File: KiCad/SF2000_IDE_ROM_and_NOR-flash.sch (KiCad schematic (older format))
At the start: 6 parts, among them J5 IDE_ATA_44pin, U13 SST39LF040, U14 SST39LF802C, U15 74LVC245A, U16 74LVC245A, U17 74LVC245A

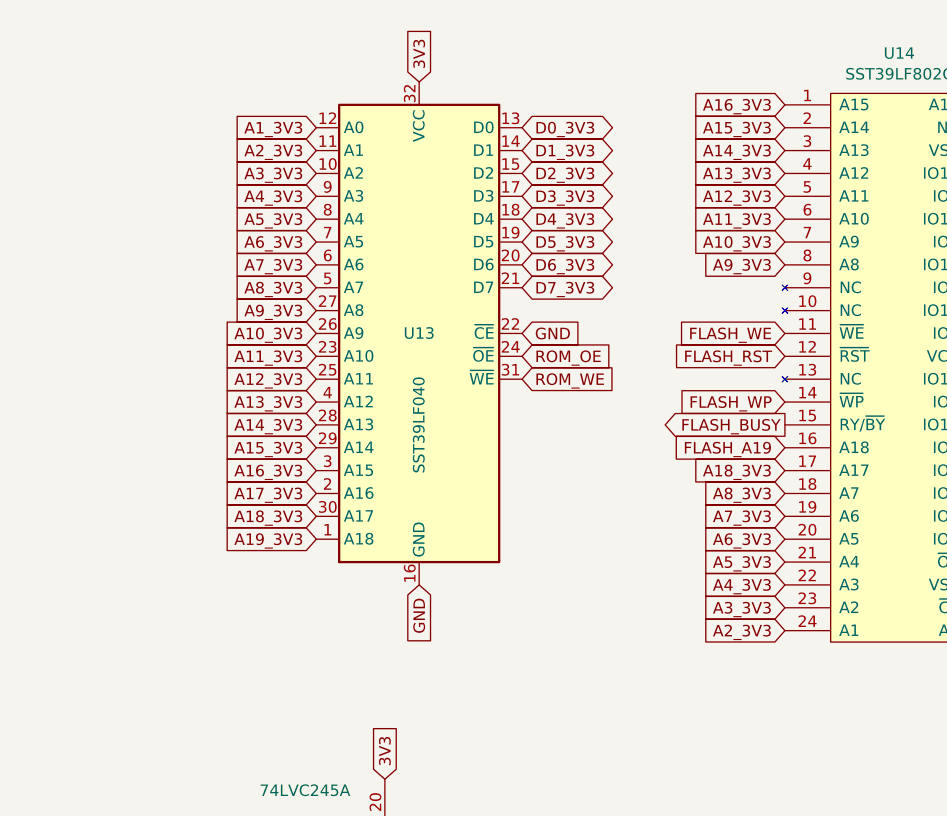
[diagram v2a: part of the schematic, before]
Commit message: added Oscillator, pull-up resistor and more routing done
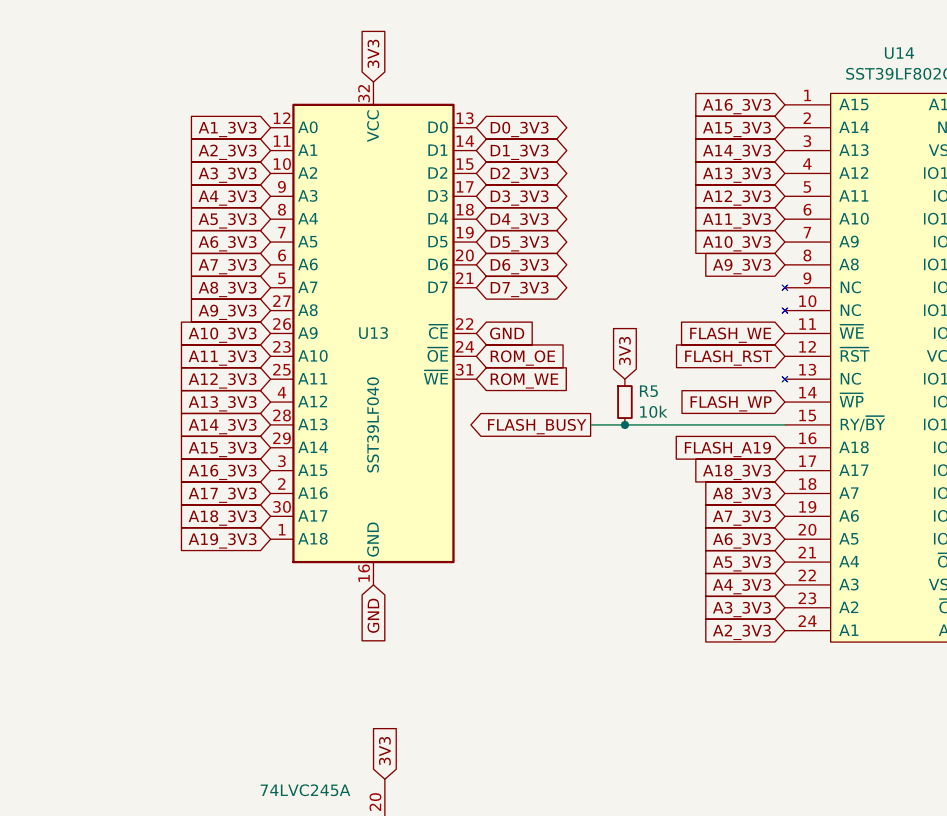
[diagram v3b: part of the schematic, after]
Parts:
- added R5: 10k, Resistor_SMD:R_0805_2012Metric_Pad1.15x1.40mm_HandSolder, symbol Device:R_Small
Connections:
- net 3V3: now also R5.1
- net FLASH_BUSY: now also R5.2
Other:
- moved on the sheet: U13
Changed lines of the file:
@@
 L SF2000:SST39LF040 U13
 U 1 1 627D2ECC
-P 6950 2600
-F 0 "U13" H 6950 2600 50  0000 C CNN
-F 1 "SST39LF040" V 6950 2200 50  0000 C CNN
-F 2 "SF2000:PLCC-32_11.4x14.0mm_P1.27mm" H 6950 2600 50  0001 C CNN
-F 3 "https://ww1.microchip.com/downloads/en/DeviceDoc/20005023B.pdf" H 6950 2700 50  0001 C CNN
-	1    6950 2600
+P 6750 2600
+F 0 "U13" H 6750 2600 50  0000 C CNN
+F 1 "SST39LF040" V 6750 2200 50  0000 C CNN
+F 2 "SF2000:PLCC-32_11.4x14.0mm_P1.27mm" H 6750 2600 50  0001 C CNN
+F 3 "https://ww1.microchip.com/downloads/en/DeviceDoc/20005023B.pdf" H 6750 2700 50  0001 C CNN
+	1    6750 2600
 	1    0    0    -1
 $EndComp
@@
 Text GLabel 9550 2700 2    50   Input ~ 0
 3V3
-Text GLabel 6500 2100 0    50   Input ~ 0
+Text GLabel 6300 2100 0    50   Input ~ 0
 A5_3V3
-Text GLabel 6500 2200 0    50   Input ~ 0
+Text GLabel 6300 2200 0    50   Input ~ 0
 A6_3V3
-Text GLabel 6500 2000 0    50   Input ~ 0
+Text GLabel 6300 2000 0    50   Input ~ 0
 A4_3V3
-Text GLabel 6500 1900 0    50   Input ~ 0
+Text GLabel 6300 1900 0    50   Input ~ 0
 A3_3V3
-Text GLabel 6500 2300 0    50   Input ~ 0
+Text GLabel 6300 2300 0    50   Input ~ 0
 A7_3V3
-Text GLabel 6500 2400 0    50   Input ~ 0
+Text GLabel 6300 2400 0    50   Input ~ 0
 A8_3V3
-Text GLabel 6500 1800 0    50   Input ~ 0
+Text GLabel 6300 1800 0    50   Input ~ 0
 A2_3V3
-Text GLabel 6500 1700 0    50   Input ~ 0
+Text GLabel 6300 1700 0    50   Input ~ 0
 A1_3V3
-Text GLabel 6500 2700 0    50   Input ~ 0
+Text GLabel 6300 2700 0    50   Input ~ 0
 A11_3V3
-Text GLabel 6500 2500 0    50   Input ~ 0
+Text GLabel 6300 2500 0    50   Input ~ 0
 A9_3V3
-Text GLabel 6500 2600 0    50   Input ~ 0
+Text GLabel 6300 2600 0    50   Input ~ 0
 A10_3V3
-Text GLabel 6500 2800 0    50   Input ~ 0
+Text GLabel 6300 2800 0    50   Input ~ 0
 A12_3V3
-Text GLabel 6500 2900 0    50   Input ~ 0
+Text GLabel 6300 2900 0    50   Input ~ 0
 A13_3V3
-Text GLabel 6500 3000 0    50   Input ~ 0
+Text GLabel 6300 3000 0    50   Input ~ 0
 A14_3V3
-Text GLabel 6500 3100 0    50   Input ~ 0
+Text GLabel 6300 3100 0    50   Input ~ 0
 A15_3V3
-Text GLabel 6500 3200 0    50   Input ~ 0
+Text GLabel 6300 3200 0    50   Input ~ 0
 A16_3V3
-Text GLabel 6500 3300 0    50   Input ~ 0
+Text GLabel 6300 3300 0    50   Input ~ 0
 A17_3V3
 Text GLabel 9550 3500 2    50   BiDi ~ 0
@@
 Text GLabel 8550 2900 0    50   Input ~ 0
 FLASH_WP
-Text GLabel 8550 3000 0    50   Output ~ 0
+Text GLabel 7700 3000 0    50   Output ~ 0
 FLASH_BUSY
-Text GLabel 7400 2800 2    50   Input ~ 0
+Text GLabel 7200 2800 2    50   Input ~ 0
 ROM_WE
-Text GLabel 7400 2700 2    50   Input ~ 0
+Text GLabel 7200 2700 2    50   Input ~ 0
 ROM_OE
-Text GLabel 7400 2600 2    50   Input ~ 0
-GND
-Text GLabel 6950 3700 3    50   Input ~ 0
-GND
-Text GLabel 6950 1500 1    50   Input ~ 0
-3V3
-Text GLabel 6500 3400 0    50   Input ~ 0
+Text GLabel 7200 2600 2    50   Input ~ 0
+GND
+Text GLabel 6750 3700 3    50   Input ~ 0
+GND
+Text GLabel 6750 1500 1    50   Input ~ 0
+3V3
+Text GLabel 6300 3400 0    50   Input ~ 0
 A18_3V3
-Text GLabel 6500 3500 0    50   Input ~ 0
+Text GLabel 6300 3500 0    50   Input ~ 0
 A19_3V3
-Text GLabel 7400 1700 2    50   BiDi ~ 0
+Text GLabel 7200 1700 2    50   BiDi ~ 0
 D0_3V3
-Text GLabel 7400 1800 2    50   BiDi ~ 0
+Text GLabel 7200 1800 2    50   BiDi ~ 0
 D1_3V3
-Text GLabel 7400 1900 2    50   BiDi ~ 0
+Text GLabel 7200 1900 2    50   BiDi ~ 0
 D2_3V3
-Text GLabel 7400 2000 2    50   BiDi ~ 0
+Text GLabel 7200 2000 2    50   BiDi ~ 0
 D3_3V3
-Text GLabel 7400 2100 2    50   BiDi ~ 0
+Text GLabel 7200 2100 2    50   BiDi ~ 0
 D4_3V3
-Text GLabel 7400 2200 2    50   BiDi ~ 0
+Text GLabel 7200 2200 2    50   BiDi ~ 0
 D5_3V3
-Text GLabel 7400 2300 2    50   BiDi ~ 0
+Text GLabel 7200 2300 2    50   BiDi ~ 0
 D6_3V3
-Text GLabel 7400 2400 2    50   BiDi ~ 0
+Text GLabel 7200 2400 2    50   BiDi ~ 0
 D7_3V3
 Text GLabel 4400 4950 0    50   BiDi ~ 0
@@
 Text GLabel 3100 2550 2    50   BiDi ~ 0
 IDE_D15
+$Comp
+L Device:R_Small R5
+U 1 1 620512F9
+P 7850 2900
+F 0 "R5" H 7909 2946 50  0000 L CNN
+F 1 "10k" H 7909 2855 50  0000 L CNN
+F 2 "Resistor_SMD:R_0805_2012Metric_Pad1.15x1.40mm_HandSolder" H 7850 2900 50  0001 C CNN
+F 3 "~" H 7850 2900 50  0001 C CNN
+	1    7850 2900
+	1    0    0    -1
+$EndComp
+Wire Wire Line
+	7700 3000 7850 3000
+Connection ~ 7850 3000
+Wire Wire Line
+	7850 3000 8550 3000
+Text GLabel 7850 2800 1    50   Input ~ 0
+3V3
 $EndSCHEMATC

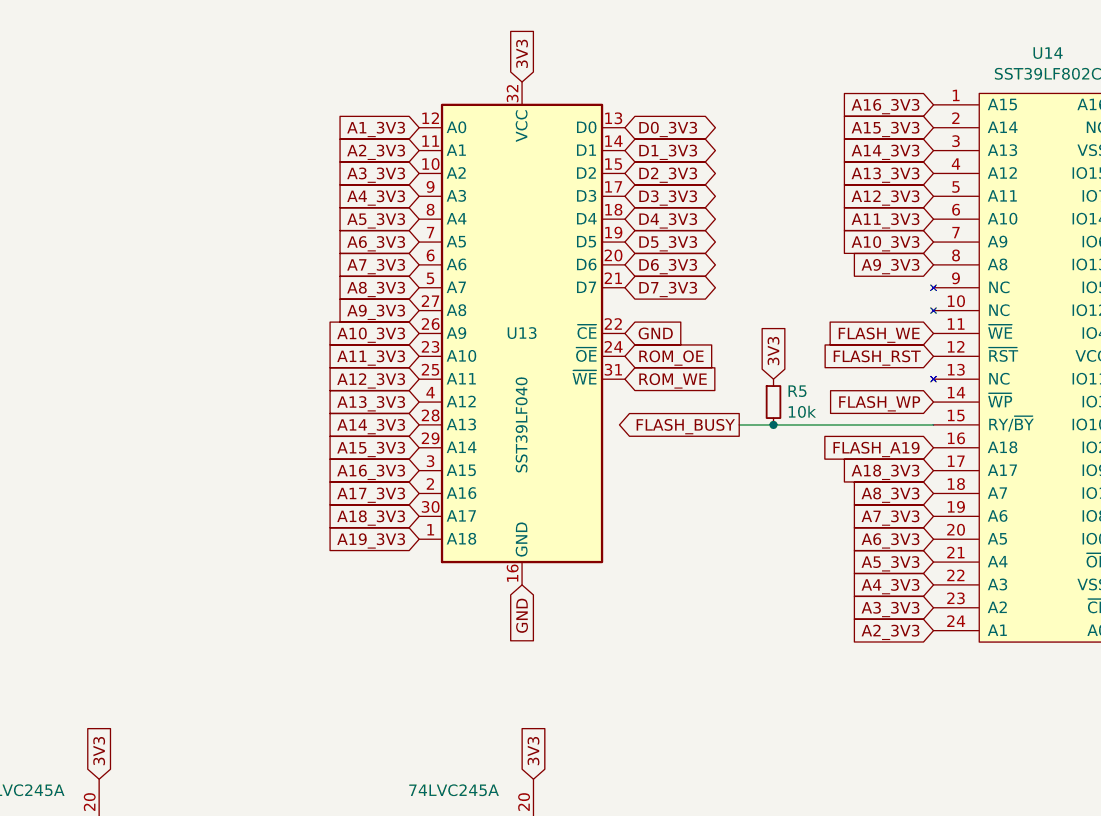
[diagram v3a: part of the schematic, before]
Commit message: more routing and fixing of FPGA pin assignments
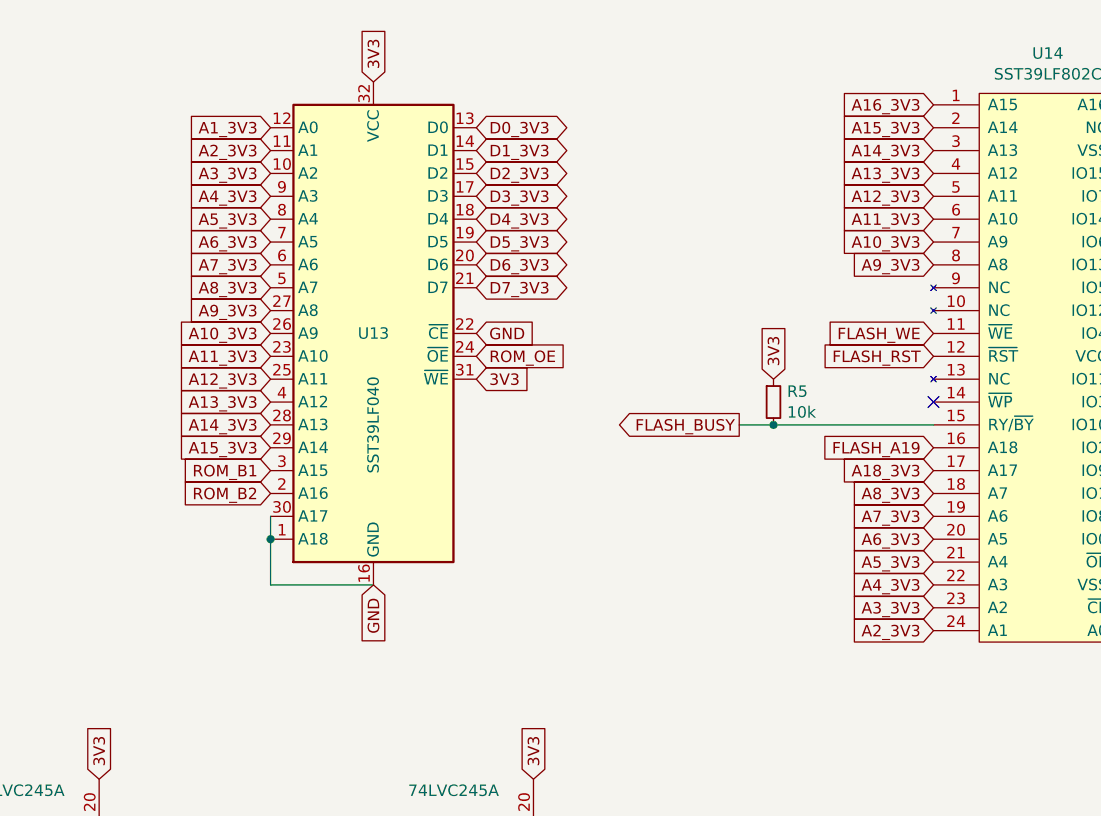
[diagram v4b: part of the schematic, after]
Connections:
- net A19_3V3 is gone; now on net GND: U13.1 (A18)
- net ROM_WE is gone; now on net 3V3: U13.31 (~WE)
- net A16_3V3: no longer U13.3 (A15)
- net A17_3V3: no longer U13.2 (A16)
- net A18_3V3: no longer U13.30 (A17)
- net GND: now also U13.30 (A17)
- net FLASH_WP: no longer names the net of U14.14 (~WP)
- new net ROM_B1: U13.3 (A15)
- new net ROM_B2: U13.2 (A16)
- no-connect marks 6 -> 7
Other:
- moved on the sheet: U13
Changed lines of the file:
@@
 L SF2000:SST39LF040 U13
 U 1 1 627D2ECC
-P 6750 2600
-F 0 "U13" H 6750 2600 50  0000 C CNN
-F 1 "SST39LF040" V 6750 2200 50  0000 C CNN
-F 2 "SF2000:PLCC-32_11.4x14.0mm_P1.27mm" H 6750 2600 50  0001 C CNN
-F 3 "https://ww1.microchip.com/downloads/en/DeviceDoc/20005023B.pdf" H 6750 2700 50  0001 C CNN
-	1    6750 2600
+P 6100 2600
+F 0 "U13" H 6100 2600 50  0000 C CNN
+F 1 "SST39LF040" V 6100 2200 50  0000 C CNN
+F 2 "SF2000:PLCC-32_11.4x14.0mm_P1.27mm" H 6100 2600 50  0001 C CNN
+F 3 "https://ww1.microchip.com/downloads/en/DeviceDoc/20005023B.pdf" H 6100 2700 50  0001 C CNN
+	1    6100 2600
 	1    0    0    -1
 $EndComp
@@
 Text GLabel 9550 2700 2    50   Input ~ 0
 3V3
-Text GLabel 6300 2100 0    50   Input ~ 0
+Text GLabel 5650 2100 0    50   Input ~ 0
 A5_3V3
-Text GLabel 6300 2200 0    50   Input ~ 0
+Text GLabel 5650 2200 0    50   Input ~ 0
 A6_3V3
-Text GLabel 6300 2000 0    50   Input ~ 0
+Text GLabel 5650 2000 0    50   Input ~ 0
 A4_3V3
-Text GLabel 6300 1900 0    50   Input ~ 0
+Text GLabel 5650 1900 0    50   Input ~ 0
 A3_3V3
-Text GLabel 6300 2300 0    50   Input ~ 0
+Text GLabel 5650 2300 0    50   Input ~ 0
 A7_3V3
-Text GLabel 6300 2400 0    50   Input ~ 0
+Text GLabel 5650 2400 0    50   Input ~ 0
 A8_3V3
-Text GLabel 6300 1800 0    50   Input ~ 0
+Text GLabel 5650 1800 0    50   Input ~ 0
 A2_3V3
-Text GLabel 6300 1700 0    50   Input ~ 0
+Text GLabel 5650 1700 0    50   Input ~ 0
 A1_3V3
-Text GLabel 6300 2700 0    50   Input ~ 0
+Text GLabel 5650 2700 0    50   Input ~ 0
 A11_3V3
-Text GLabel 6300 2500 0    50   Input ~ 0
+Text GLabel 5650 2500 0    50   Input ~ 0
 A9_3V3
-Text GLabel 6300 2600 0    50   Input ~ 0
+Text GLabel 5650 2600 0    50   Input ~ 0
 A10_3V3
-Text GLabel 6300 2800 0    50   Input ~ 0
+Text GLabel 5650 2800 0    50   Input ~ 0
 A12_3V3
-Text GLabel 6300 2900 0    50   Input ~ 0
+Text GLabel 5650 2900 0    50   Input ~ 0
 A13_3V3
-Text GLabel 6300 3000 0    50   Input ~ 0
+Text GLabel 5650 3000 0    50   Input ~ 0
 A14_3V3
-Text GLabel 6300 3100 0    50   Input ~ 0
+Text GLabel 5650 3100 0    50   Input ~ 0
 A15_3V3
-Text GLabel 6300 3200 0    50   Input ~ 0
-A16_3V3
-Text GLabel 6300 3300 0    50   Input ~ 0
-A17_3V3
+Text GLabel 5650 3200 0    50   Input ~ 0
+ROM_B1
+Text GLabel 5650 3300 0    50   Input ~ 0
+ROM_B2
 Text GLabel 9550 3500 2    50   BiDi ~ 0
 D0_3V3
@@
 Text GLabel 8550 2700 0    50   Input ~ 0
 FLASH_RST
-Text GLabel 8550 2900 0    50   Input ~ 0
-FLASH_WP
 Text GLabel 7700 3000 0    50   Output ~ 0
 FLASH_BUSY
-Text GLabel 7200 2800 2    50   Input ~ 0
-ROM_WE
-Text GLabel 7200 2700 2    50   Input ~ 0
+Text GLabel 6550 2700 2    50   Input ~ 0
 ROM_OE
-Text GLabel 7200 2600 2    50   Input ~ 0
-GND
-Text GLabel 6750 3700 3    50   Input ~ 0
-GND
-Text GLabel 6750 1500 1    50   Input ~ 0
-3V3
-Text GLabel 6300 3400 0    50   Input ~ 0
-A18_3V3
-Text GLabel 6300 3500 0    50   Input ~ 0
-A19_3V3
-Text GLabel 7200 1700 2    50   BiDi ~ 0
+Text GLabel 6550 2600 2    50   Input ~ 0
+GND
+Text GLabel 6100 3700 3    50   Input ~ 0
+GND
+Text GLabel 6100 1500 1    50   Input ~ 0
+3V3
+Text GLabel 6550 1700 2    50   BiDi ~ 0
 D0_3V3
-Text GLabel 7200 1800 2    50   BiDi ~ 0
+Text GLabel 6550 1800 2    50   BiDi ~ 0
 D1_3V3
-Text GLabel 7200 1900 2    50   BiDi ~ 0
+Text GLabel 6550 1900 2    50   BiDi ~ 0
 D2_3V3
-Text GLabel 7200 2000 2    50   BiDi ~ 0
+Text GLabel 6550 2000 2    50   BiDi ~ 0
 D3_3V3
-Text GLabel 7200 2100 2    50   BiDi ~ 0
+Text GLabel 6550 2100 2    50   BiDi ~ 0
 D4_3V3
-Text GLabel 7200 2200 2    50   BiDi ~ 0
+Text GLabel 6550 2200 2    50   BiDi ~ 0
 D5_3V3
-Text GLabel 7200 2300 2    50   BiDi ~ 0
+Text GLabel 6550 2300 2    50   BiDi ~ 0
 D6_3V3
-Text GLabel 7200 2400 2    50   BiDi ~ 0
+Text GLabel 6550 2400 2    50   BiDi ~ 0
 D7_3V3
 Text GLabel 4400 4950 0    50   BiDi ~ 0
@@
 Text GLabel 7850 2800 1    50   Input ~ 0
 3V3
+Wire Wire Line
+	6100 3700 5650 3700
+Wire Wire Line
+	5650 3700 5650 3500
+Connection ~ 5650 3500
+Wire Wire Line
+	5650 3500 5650 3400
+Text GLabel 6550 2800 2    50   Input ~ 0
+3V3
+NoConn ~ 8550 2900
 $EndSCHEMATC

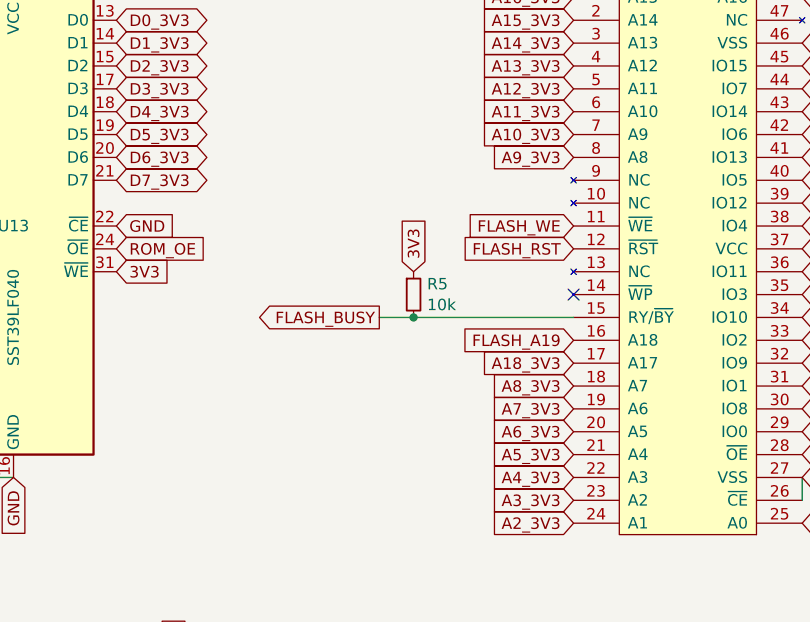
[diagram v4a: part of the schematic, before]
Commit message: more routing and fixed pull-up resistors for Flash mem control signals
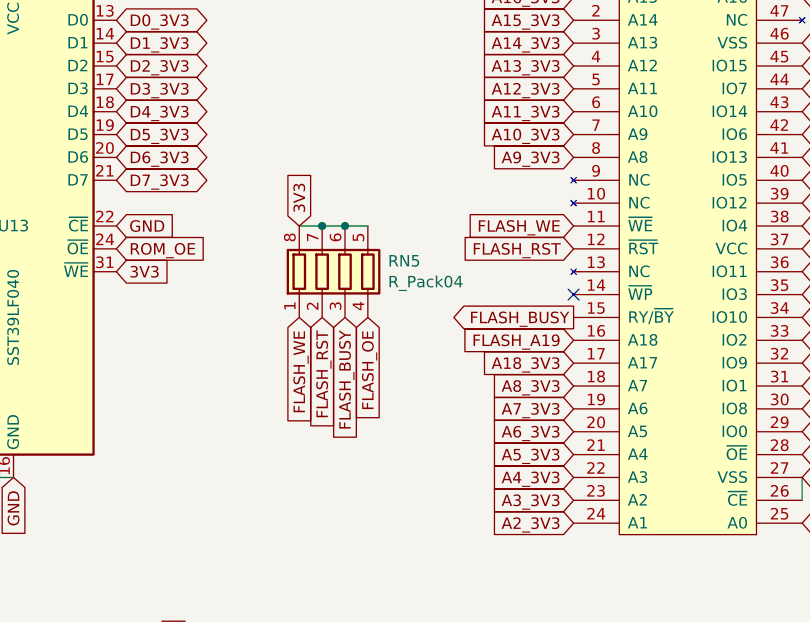
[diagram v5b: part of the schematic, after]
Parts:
- removed R5: 10k, Resistor_SMD:R_0805_2012Metric_Pad1.15x1.40mm_HandSolder, symbol Device:R_Small
- added RN5: R_Pack04, SF2000:RESCAF80P320X160X60-8N, symbol Device:R_Pack04
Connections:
- net 3V3: now also RN5.5 (R4.2), RN5.6 (R3.2), RN5.7 (R2.2), RN5.8 (R1.2)
- net FLASH_BUSY: now also RN5.3 (R3.1)
- net FLASH_OE: now also RN5.4 (R4.1)
- net FLASH_RST: now also RN5.2 (R2.1)
- net FLASH_WE: now also RN5.1 (R1.1)
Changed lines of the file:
@@
 Text GLabel 8550 2700 0    50   Input ~ 0
 FLASH_RST
-Text GLabel 7700 3000 0    50   Output ~ 0
+Text GLabel 8550 3000 0    50   Output ~ 0
 FLASH_BUSY
 Text GLabel 6550 2700 2    50   Input ~ 0
@@
 Text GLabel 3100 2550 2    50   BiDi ~ 0
 IDE_D15
+Wire Wire Line
+	6100 3700 5650 3700
+Wire Wire Line
+	5650 3700 5650 3500
+Connection ~ 5650 3500
+Wire Wire Line
+	5650 3500 5650 3400
+Text GLabel 6550 2800 2    50   Input ~ 0
+3V3
+NoConn ~ 8550 2900
 $Comp
-L Device:R_Small R5
-U 1 1 620512F9
-P 7850 2900
-F 0 "R5" H 7909 2946 50  0000 L CNN
-F 1 "10k" H 7909 2855 50  0000 L CNN
-F 2 "Resistor_SMD:R_0805_2012Metric_Pad1.15x1.40mm_HandSolder" H 7850 2900 50  0001 C CNN
-F 3 "~" H 7850 2900 50  0001 C CNN
-	1    7850 2900
+L Device:R_Pack04 RN?
+U 1 1 6206820D
+P 7550 2800
+AR Path="/620D263D/6206820D" Ref="RN?"  Part="1"
+AR Path="/627A6500/6206820D" Ref="RN5"  Part="1"
+F 0 "RN5" H 7738 2846 50  0000 L CNN
+F 1 "R_Pack04" H 7738 2755 50  0000 L CNN
+F 2 "SF2000:RESCAF80P320X160X60-8N" V 7825 2800 50  0001 C CNN
+F 3 "~" H 7550 2800 50  0001 C CNN
+	1    7550 2800
 	1    0    0    -1
 $EndComp
-Wire Wire Line
-	7700 3000 7850 3000
-Connection ~ 7850 3000
-Wire Wire Line
-	7850 3000 8550 3000
-Text GLabel 7850 2800 1    50   Input ~ 0
-3V3
-Wire Wire Line
-	6100 3700 5650 3700
-Wire Wire Line
-	5650 3700 5650 3500
-Connection ~ 5650 3500
-Wire Wire Line
-	5650 3500 5650 3400
-Text GLabel 6550 2800 2    50   Input ~ 0
-3V3
-NoConn ~ 8550 2900
+Text GLabel 7350 2600 1    50   Input ~ 0
+3V3
+Wire Wire Line
+	7350 2600 7450 2600
+Connection ~ 7450 2600
+Wire Wire Line
+	7450 2600 7550 2600
+Connection ~ 7550 2600
+Wire Wire Line
+	7550 2600 7650 2600
+Text GLabel 7350 3000 3    50   Input ~ 0
+FLASH_WE
+Text GLabel 7450 3000 3    50   Input ~ 0
+FLASH_RST
+Text GLabel 7550 3000 3    50   Input ~ 0
+FLASH_BUSY
+Text GLabel 7650 3000 3    50   Input ~ 0
+FLASH_OE
 $EndSCHEMATC
